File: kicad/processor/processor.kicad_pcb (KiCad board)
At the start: 4 copper layers, 75 x 50 mm, 95 parts, among them J101 CONN_02X07, J201 V_QI, J202 GND, J203 Battery, M401 MICROSD, Q201 DMG3415U, Q202 DMG3415U, Q203 DMG3414U, Q204 DMG3415U, Q205 DMG3415U, Q301 DMG3415U, Q401 DMG3415U, Q501 MMBT4401, Q502 MMBT4401, SW201 SW, SW501 SWITCH_PUSHBUTTON, SW502 SWITCH_PUSHBUTTON, U101 ESP32-WROOM, U102 BME280, U103 TCA9534A, U201 MCP73832, U202 NCP694-3.3, U301 FGPMMOPA6H, U501 USB_B_Socket, U502 SP3003-04, U503 CP2102N

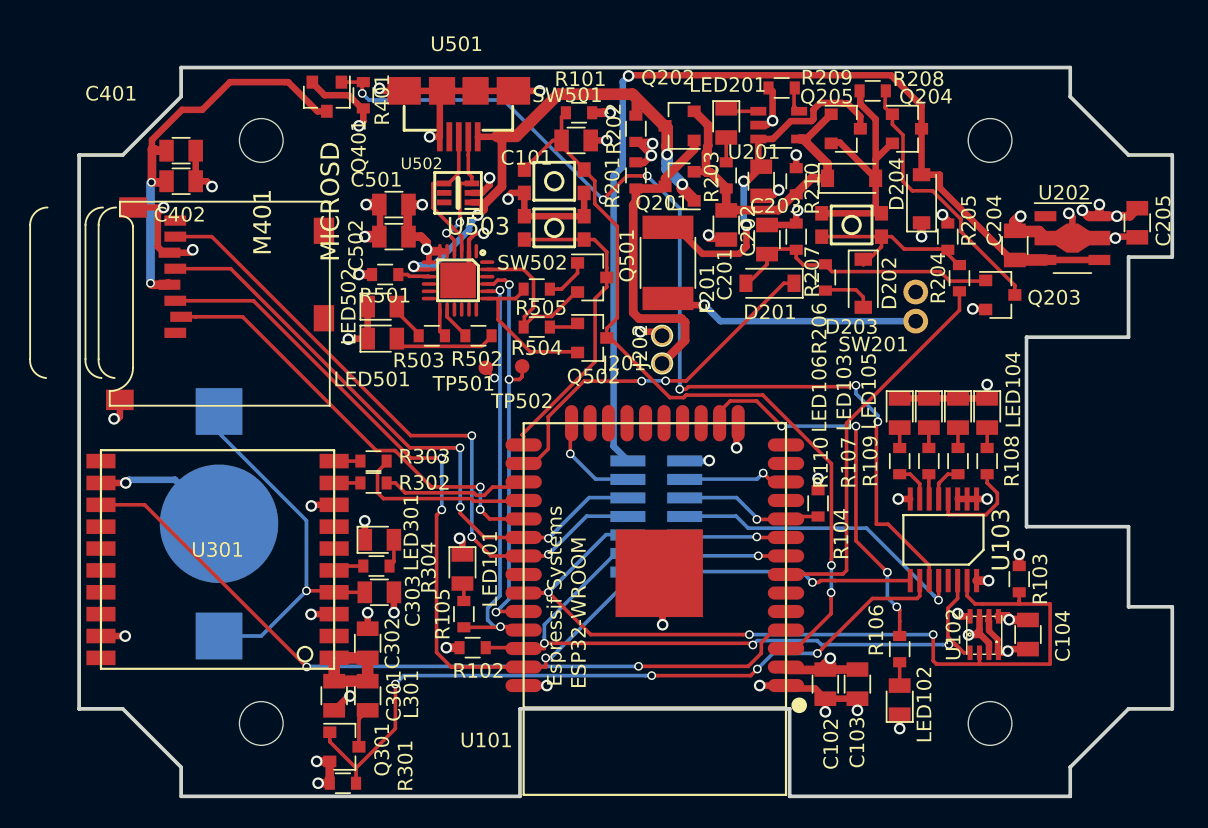
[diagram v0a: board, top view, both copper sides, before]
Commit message: RC3 Fix vias too close to edge
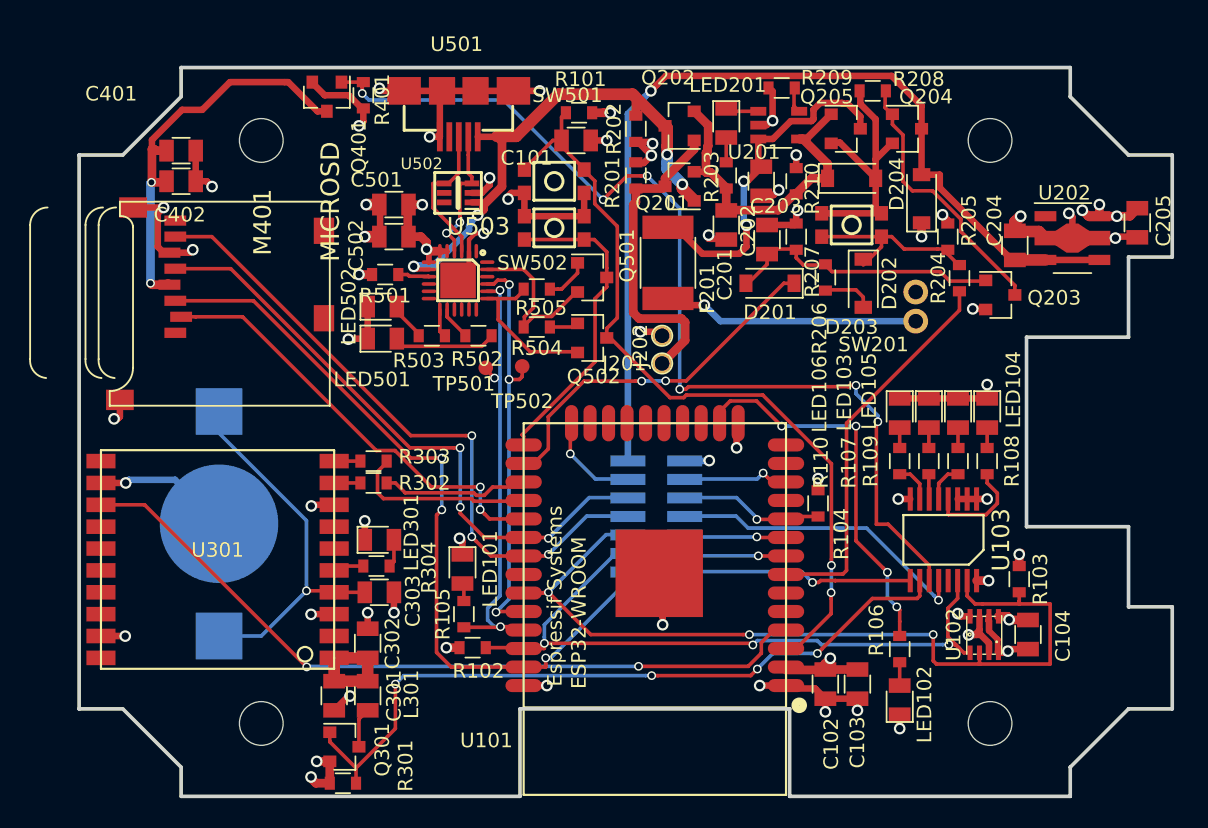
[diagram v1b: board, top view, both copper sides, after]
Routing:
- net /+V_UNREG_SW: track 68.2 -> 65.8 mm
- net +3V3: track 39.9 -> 40.6 mm
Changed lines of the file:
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@@
     (links 233)
     (no_connects 0)
-    (area -3.57766 -2.525 77.5 52.5)
+    (area -0.127001 -0.127001 75.125001 50.127001)
     (thickness 1.6)
     (drawings 50)
-    (tracks 958)
+    (tracks 959)
     (zones 0)
     (modules 95)
@@
   (gr_line (start 0 6) (end 0 44) (layer Edge.Cuts) (width 0.254))
   (gr_line (start 68 0) (end 7 0) (layer Edge.Cuts) (width 0.254))
+  (segment (start 15.913622 48.763622) (end 15.913622 48.673497) (width 0.6) (layer F.Cu) (net 1))
+  (segment (start 16.25 49.1) (end 15.913622 48.763622) (width 0.6) (layer F.Cu) (net 1))
+  (segment (start 17.2 49.1) (end 16.25 49.1) (width 0.6) (layer F.Cu) (net 1))
+  (via (at 15.913622 48.673497) (size 0.8) (drill 0.5) (layers F.Cu B.Cu) (net 1))
   (segment (start 19.5 2.8) (end 19.5 3.7) (width 0.45) (layer F.Cu) (net 1))
   (segment (start 19.5 3.7) (end 19.2 4) (width 0.45) (layer F.Cu) (net 1))
@@
   (segment (start 17.2 47.6) (end 16.3 47.6) (width 0.6) (layer F.Cu) (net 1))
   (via (at 16.3 47.6) (size 0.8) (drill 0.5) (layers F.Cu B.Cu) (net 1))
-  (via (at 16.4 49.1) (size 0.8) (drill 0.5) (layers F.Cu B.Cu) (net 1))
-  (segment (start 17.2 49.1) (end 16.4 49.1) (width 0.6) (layer F.Cu) (net 1))
   (segment (start 17.2 47.6) (end 17.2 49.1) (width 0.6) (layer F.Cu) (net 1))
   (segment (start 22.55 11.6) (end 23.45 11.6) (width 0.6) (layer F.Cu) (net 1))
@@
   (segment (start 48.35 14.8) (end 49.05 14.8) (width 0.25) (layer F.Cu) (net 4))
   (via (at 40.242218 21.495702) (size 0.6) (drill 0.4) (layers F.Cu B.Cu) (net 4))
-  (segment (start 37.65 26.965) (end 36.669376 25.984376) (width 0.45) (layer B.Cu) (net 5))
-  (segment (start 36.669376 25.984376) (end 36.669376 7.431109) (width 0.45) (layer B.Cu) (net 5))
-  (segment (start 36.669376 7.431109) (end 37.300001 6.800484) (width 0.45) (layer B.Cu) (net 5))
-  (segment (start 37.300001 0.974998) (end 37.7 0.574999) (width 0.45) (layer B.Cu) (net 5))
-  (segment (start 37.300001 6.800484) (end 37.300001 0.974998) (width 0.45) (layer B.Cu) (net 5))
-  (segment (start 37.7 0.574999) (end 37.745682 0.529317) (width 0.45) (layer F.Cu) (net 5))
-  (segment (start 37.745682 0.529317) (end 55.704319 0.529317) (width 0.45) (layer F.Cu) (net 5))
-  (segment (start 55.704319 0.529317) (end 57.8 2.624998) (width 0.45) (layer F.Cu) (net 5))
-  (segment (start 57.8 2.624998) (end 57.8 4.2) (width 0.45) (layer F.Cu) (net 5))
-  (via (at 37.7 0.574999) (size 0.8) (drill 0.5) (layers F.Cu B.Cu) (net 5))
+  (segment (start 40.254096 0.571533) (end 39.627152 1.198477) (width 0.45) (layer F.Cu) (net 5))
+  (segment (start 57.8 2.624998) (end 55.746535 0.571533) (width 0.45) (layer F.Cu) (net 5))
+  (segment (start 57.8 4.2) (end 57.8 2.624998) (width 0.45) (layer F.Cu) (net 5))
+  (segment (start 55.746535 0.571533) (end 40.254096 0.571533) (width 0.45) (layer F.Cu) (net 5))
+  (segment (start 38.827154 1.998475) (end 39.227153 1.598476) (width 0.45) (layer B.Cu) (net 5))
+  (segment (start 39.627152 1.198477) (end 39.227153 1.598476) (width 0.45) (layer F.Cu) (net 5))
+  (segment (start 37.65 3.175629) (end 38.827154 1.998475) (width 0.45) (layer B.Cu) (net 5))
+  (segment (start 37.65 26.965) (end 37.65 3.175629) (width 0.45) (layer B.Cu) (net 5))
+  (via (at 39.227153 1.598476) (size 0.8) (drill 0.5) (layers F.Cu B.Cu) (net 5))
   (segment (start 59.05 8.25) (end 59.05 7.35) (width 0.45) (layer F.Cu) (net 5))
   (segment (start 64.2 13.15) (end 63.95 13.15) (width 0.45) (layer F.Cu) (net 5))

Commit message: Switch to nightly Windows build
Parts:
- renumbered REF** to ?
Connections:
- M401 pad 1: (no net) -> Net-(M401-Pad1)
- M401 pad 8: (no net) -> Net-(M401-Pad8)
- M401 pad CD1: (no net) -> Net-(M401-PadCD1)
- M401 pad CD2: (no net) -> Net-(M401-PadCD2)
- U101 pad 11: (no net) -> Net-(U101-Pad11)
- U101 pad 13: (no net) -> Net-(U101-Pad13)
- U101 pad 14: (no net) -> Net-(U101-Pad14)
- U101 pad 17: (no net) -> Net-(U101-Pad17)
- U101 pad 18: (no net) -> Net-(U101-Pad18)
- U101 pad 19: (no net) -> Net-(U101-Pad19)
- U101 pad 20: (no net) -> Net-(U101-Pad20)
- U101 pad 21: (no net) -> Net-(U101-Pad21)
- U101 pad 22: (no net) -> Net-(U101-Pad22)
- U101 pad 23: (no net) -> Net-(U101-Pad23)
- U101 pad 32: (no net) -> Net-(U101-Pad32)
- U101 pad 5: (no net) -> Net-(U101-Pad5)
- U101 pad 6: (no net) -> Net-(U101-Pad6)
- U103 pad 13: (no net) -> Net-(U103-Pad13)
- U202 pad 1: (no net) -> Net-(U202-Pad1)
- U301 pad 11: (no net) -> Net-(U301-Pad11)
- U301 pad 14: (no net) -> Net-(U301-Pad14)
- U301 pad 15: (no net) -> Net-(U301-Pad15)
- U301 pad 16: (no net) -> Net-(U301-Pad16)
- U301 pad 17: (no net) -> Net-(U301-Pad17)
- U301 pad 18: (no net) -> Net-(U301-Pad18)
- U301 pad 20: (no net) -> Net-(U301-Pad20)
- U501 pad 4: (no net) -> Net-(U501-Pad4)
- U502 pad 5: (no net) -> Net-(U502-Pad5)
- U502 pad 6: (no net) -> Net-(U502-Pad6)
- U503 pad 1: (no net) -> Net-(U503-Pad1)
- U503 pad 10: (no net) -> Net-(U503-Pad10)
- U503 pad 11: (no net) -> Net-(U503-Pad11)
- U503 pad 12: (no net) -> Net-(U503-Pad12)
- U503 pad 15: (no net) -> Net-(U503-Pad15)
- U503 pad 16: (no net) -> Net-(U503-Pad16)
- U503 pad 17: (no net) -> Net-(U503-Pad17)
- U503 pad 18: (no net) -> Net-(U503-Pad18)
- U503 pad 22: (no net) -> Net-(U503-Pad22)
- U503 pad 24: (no net) -> Net-(U503-Pad24)

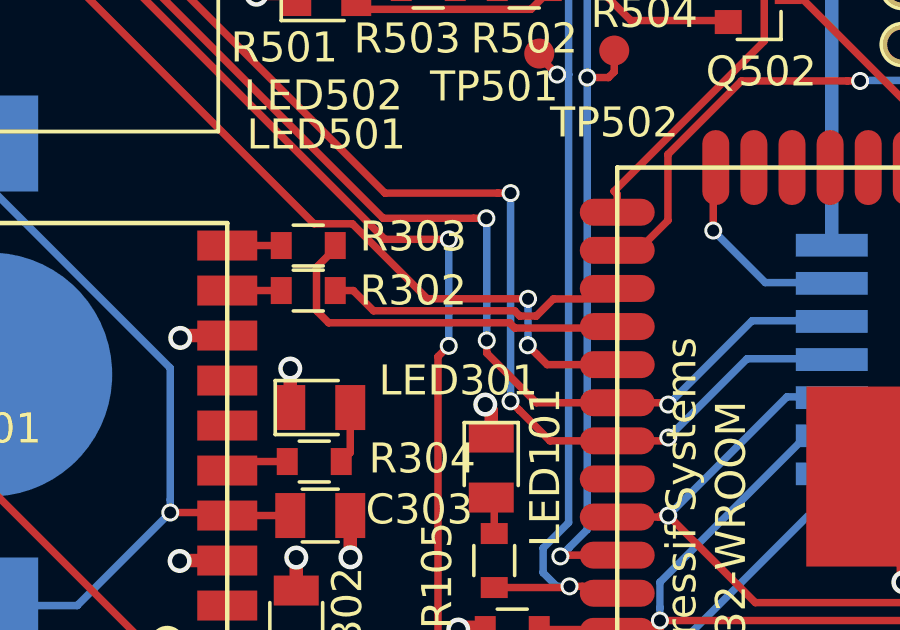
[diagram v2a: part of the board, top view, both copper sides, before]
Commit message: Fix updated connector footprint
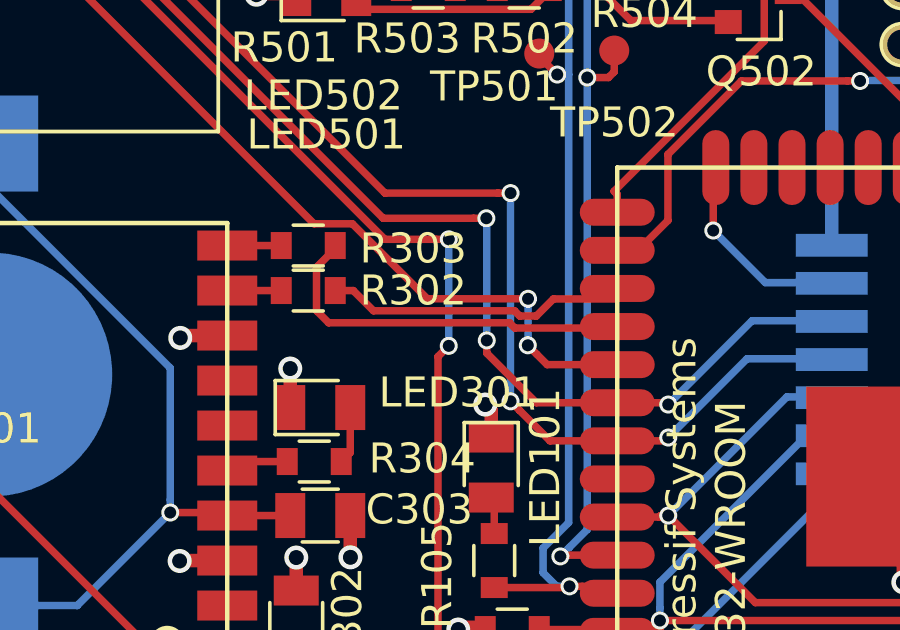
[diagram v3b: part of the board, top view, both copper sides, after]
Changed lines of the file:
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@@
     (43 Eco2.User user)
     (44 Edge.Cuts user)
-    (45 Margin user)
-    (46 B.CrtYd user)
-    (47 F.CrtYd user)
-    (48 B.Fab user)
-    (49 F.Fab user)
+    (45 Margin user hide)
+    (46 B.CrtYd user hide)
+    (47 F.CrtYd user hide)
+    (48 B.Fab user hide)
+    (49 F.Fab user hide)
   )
   (setup
@@
     (tags "SMD 0805 DIODE LED")
     (attr smd)
-    (fp_text reference LED301 (at 4.6 -0.9) (layer F.SilkS)
+    (fp_text reference LED301 (at 4.6 -0.5) (layer F.SilkS)
       (effects (font (size 1 1) (thickness 0.15)))
     )
@@
     (tags "resistor 0603")
     (attr smd)
-    (fp_text reference R303 (at -3.5 0.3 180) (layer F.SilkS)
+    (fp_text reference R303 (at -3.5 -0.1) (layer F.SilkS)
       (effects (font (size 1 1) (thickness 0.15)))
     )
@@
     (tags "resistor 0603")
     (attr smd)
-    (fp_text reference R302 (at -3.5 0 180) (layer F.SilkS)
-      (effects (font (size 1 1) (thickness 0.15)))
-    )
+    (fp_text reference R302 (at -3.5 0) (layer F.SilkS)
+      (effects (font (size 1 1) (thickness 0.15)))
+    )
